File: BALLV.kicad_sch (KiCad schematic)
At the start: 3 parts

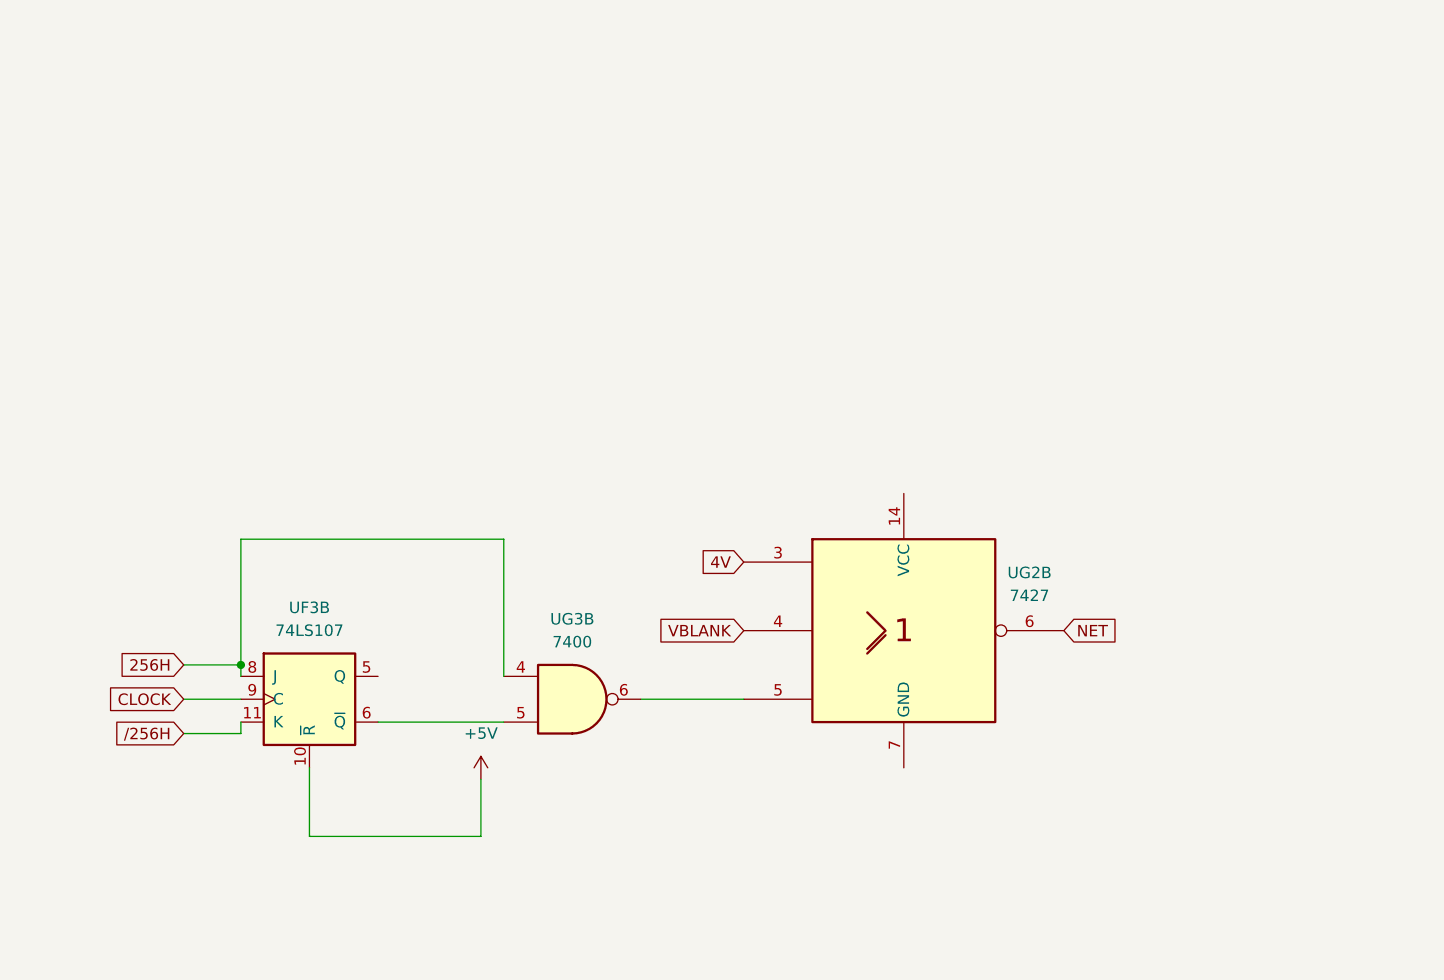
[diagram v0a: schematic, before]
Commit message: Added remainder of sheets
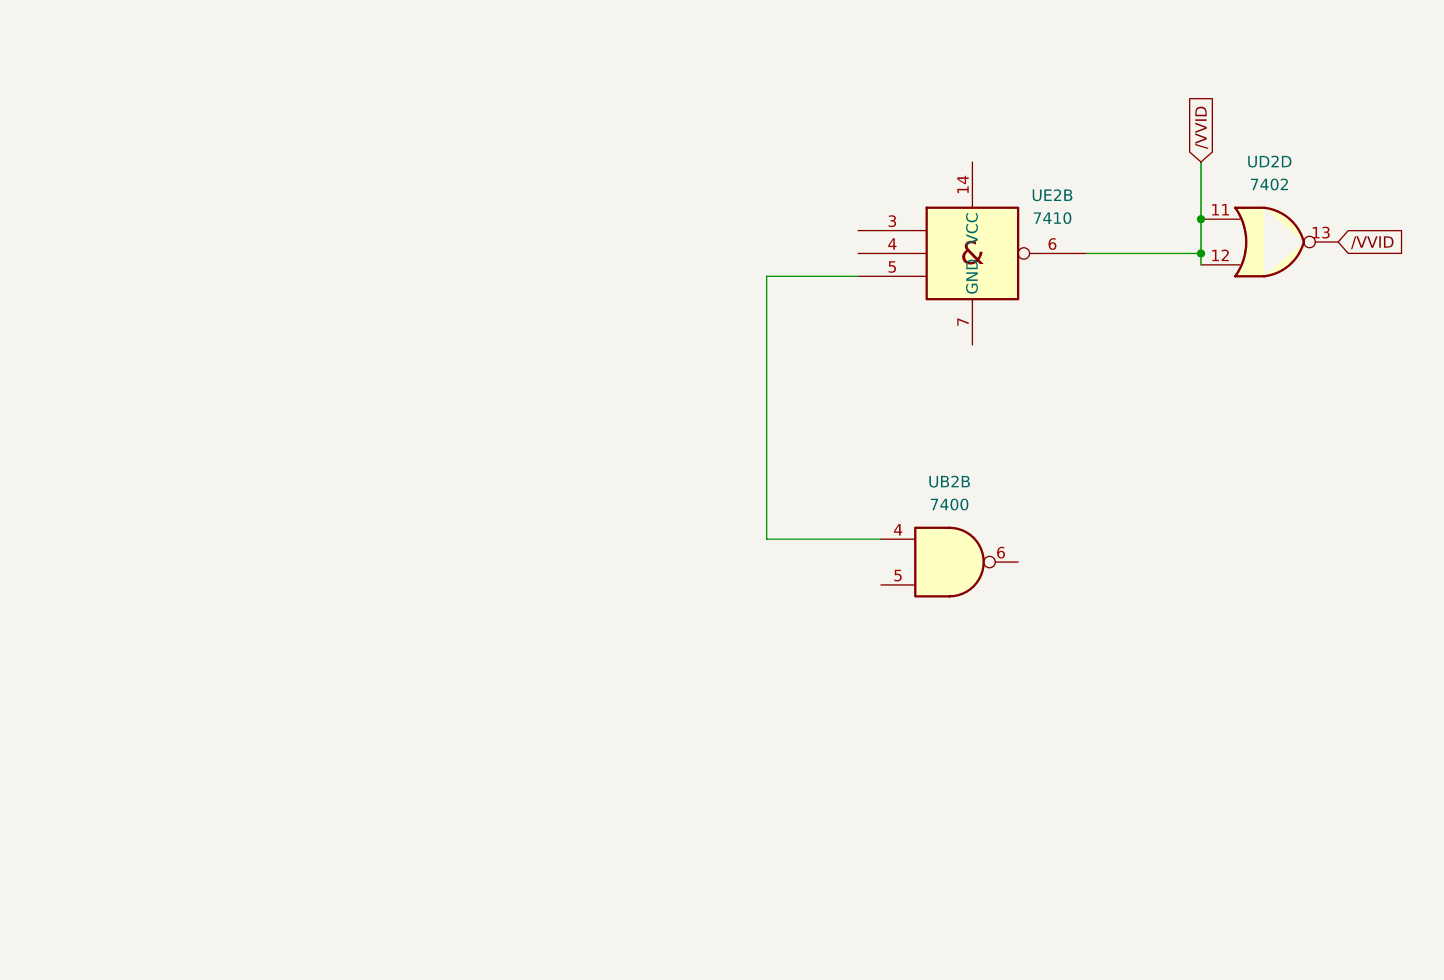
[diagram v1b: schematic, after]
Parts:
- removed UF3: 74LS107, Package_DIP:DIP-14_W7.62mm_Socket_LongPads, symbol 74xx:74LS107
- removed UG2: 7427, Package_DIP:DIP-14_W7.62mm_Socket_LongPads, symbol 74xx_IEEE:7427
- removed UG3: 7400, Package_DIP:DIP-14_W7.62mm_Socket_LongPads, symbol 74xx:7400
- added UB2: 7400, Package_DIP:DIP-14_W7.62mm_Socket_LongPads, symbol 74xx:7400
- added UD2: 7402, Package_DIP:DIP-14_W7.62mm_Socket_LongPads, symbol 74xx:7402
- added UE2: 7410, Package_DIP:DIP-14_W7.62mm_Socket_LongPads, symbol 74xx_IEEE:7410
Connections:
- new net: UB2.4, UE2.5
- new net /VVID: UD2.11, UD2.12, UD2.13, UE2.6

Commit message: R20260915
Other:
- company: (none) -> Atari
- title: (none) -> PONG
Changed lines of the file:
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@@
 	(generator "eeschema")
 	(generator_version "10.0")
-	(paper "A4")
+	(paper "USLetter")
+	(title_block
+		(title "PONG")
+		(company "Atari")
+	)
 	(junction
 		(at 193.04 50.8)

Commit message: R20260918
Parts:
- UB2, UD2, UE2: footprint Package_DIP:DIP-14_W7.62mm_Socket_LongPads -> pong:pong_DIP-14_W7.62mm_Socket_LongPads
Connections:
- net /VVID: no longer UD2.13
- net +3.3V: now reaches UE2.14 (VCC)
- net GND: now reaches UE2.7 (GND)
- new net VVID: UD2.13
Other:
- note added: "NEED 9316 ICS"
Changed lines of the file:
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@@
 		(company "Atari")
 	)
-	(junction
-		(at 193.04 50.8)
-		(diameter 0)
-		(color 0 0 0 0)
+	(text "NEED 9316 ICS"
+		(exclude_from_sim no)
+		(at 70.104 101.346 0)
+		(effects
+			(font
+				(size 1.27 1.27)
+			)
+		)
 	)
 	(junction
@@
 	(wire
 		(pts
-			(xy 193.04 44.45) (xy 193.04 50.8)
+			(xy 154.94 57.15) (xy 144.78 57.15)
 		)
 		(stroke
@@
 		)
 	)
-	(wire
-		(pts
-			(xy 154.94 57.15) (xy 144.78 57.15)
-		)
-		(stroke
-			(width 0)
-			(type default)
-		)
-	)
 	(global_label "{slash}VVID"
 		(shape input)
-		(at 193.04 44.45 90)
+		(at 193.04 50.8 90)
 		(fields_autoplaced yes)
 		(effects
@@
 		)
 		(property "Intersheetrefs" "${INTERSHEET_REFS}"
-			(at 193.04 36.0823 90)
+			(at 193.04 42.4323 90)
 			(hide yes)
 			(show_name no)
@@
 		)
 	)
-	(global_label "{slash}VVID"
+	(global_label "VVID"
 		(shape input)
 		(at 208.28 53.34 0)
@@
 			)
 		)
-		(property "Footprint" "Package_DIP:DIP-14_W7.62mm_Socket_LongPads"
+		(property "Footprint" "pong:pong_DIP-14_W7.62mm_Socket_LongPads"
 			(at 200.66 53.34 0)
 			(hide yes)
@@
 					(reference "UD2")
 					(unit 4)
+				)
+			)
+		)
+	)
+	(symbol
+		(lib_id "power:GND")
+		(at 167.64 64.77 0)
+		(unit 1)
+		(body_style 1)
+		(exclude_from_sim no)
+		(in_bom yes)
+		(on_board yes)
+		(in_pos_files yes)
+		(dnp no)
+		(property "Reference" "#PWR0143"
+			(at 167.64 71.12 0)
+			(hide yes)
+			(show_name no)
+			(do_not_autoplace no)
+			(effects
+				(font
+					(size 1.27 1.27)
+				)
+			)
+		)
+		(property "Value" "GND"
+			(at 170.434 63.754 90)
+			(show_name no)
+			(do_not_autoplace no)
+			(effects
+				(font
+					(size 1.27 1.27)
+				)
+				(justify right)
+			)
+		)
+		(property "Footprint" ""
+			(at 167.64 64.77 0)
+			(hide yes)
+			(show_name no)
+			(do_not_autoplace no)
+			(effects
+				(font
+					(size 1.27 1.27)
+				)
+			)
+		)
+		(property "Datasheet" ""
+			(at 167.64 64.77 0)
+			(hide yes)
+			(show_name no)
+			(do_not_autoplace no)
+			(effects
+				(font
+					(size 1.27 1.27)
+				)
+			)
+		)
+		(property "Description" "Power symbol creates a global label with name \"GND\" , ground"
+			(at 167.64 64.77 0)
+			(hide yes)
+			(show_name no)
+			(do_not_autoplace no)
+			(effects
+				(font
+					(size 1.27 1.27)
+				)
+			)
+		)
+		(pin "1"
+		)
+		(instances
+			(project "pong"
+				(path "/6c55baa6-be38-444e-ac95-9cecf812b759/77c55ca7-a066-4d98-a4d1-18b720a3c31f"
+					(reference "#PWR0143")
+					(unit 1)
 				)
 			)
@@
 			)
 		)
-		(property "Footprint" "Package_DIP:DIP-14_W7.62mm_Socket_LongPads"
+		(property "Footprint" "pong:pong_DIP-14_W7.62mm_Socket_LongPads"
 			(at 165.1 88.9 0)
 			(hide yes)
@@
 			)
 		)
-		(property "Footprint" "Package_DIP:DIP-14_W7.62mm_Socket_LongPads"
+		(property "Footprint" "pong:pong_DIP-14_W7.62mm_Socket_LongPads"
 			(at 167.64 54.61 0)
 			(hide yes)
@@
 				)
 			)
+		)
+	)
+	(symbol
+		(lib_id "power:VCC")
+		(at 167.64 44.45 0)
+		(unit 1)
+		(body_style 1)
+		(exclude_from_sim no)
+		(in_bom yes)
+		(on_board yes)
+		(in_pos_files yes)
+		(dnp no)
+		(fields_autoplaced yes)
+		(property "Reference" "#PWR0142"
+			(at 167.64 48.26 0)
+			(hide yes)
+			(show_name no)
+			(do_not_autoplace no)
+			(effects
+				(font
+					(size 1.27 1.27)
+				)
+			)
+		)
+		(property "Value" "+3.3V"
+			(at 167.6399 40.64 90)
+			(show_name no)
+			(do_not_autoplace no)
+			(effects
+				(font
+					(size 1.27 1.27)
+				)
+				(justify left)
+			)
+		)
+		(property "Footprint" ""
+			(at 167.64 44.45 0)
+			(hide yes)
+			(show_name no)
+			(do_not_autoplace no)
+			(effects
+				(font
+					(size 1.27 1.27)
+				)
+			)
+		)
+		(property "Datasheet" ""
+			(at 167.64 44.45 0)
+			(hide yes)
+			(show_name no)
+			(do_not_autoplace no)
+			(effects
+				(font
+					(size 1.27 1.27)
+				)
+			)
+		)
+		(property "Description" "Power symbol creates a global label with name \"VCC\""
+			(at 167.64 44.45 0)
+			(hide yes)
+			(show_name no)
+			(do_not_autoplace no)
+			(effects
+				(font
+					(size 1.27 1.27)
+				)
+			)
+		)
+		(pin "1"
+		)
+		(instances
+			(project "pong"
+				(path "/6c55baa6-be38-444e-ac95-9cecf812b759/77c55ca7-a066-4d98-a4d1-18b720a3c31f"
+					(reference "#PWR0142")
+					(unit 1)
+				)
+			)

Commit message: R20260922PM
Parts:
- added UA3, UB3: 74LS161, pong:pong_DIP-16_W7.62mm_Socket_LongPads, symbol 74xx:74LS161
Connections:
- net +3.3V: now also UA3.16 (VCC), UB3.16 (VCC)
- net GND: now also UA3.3 (D0), UA3.4 (D1), UA3.5 (D2), UA3.6 (D3), UA3.8 (GND), UB3.8 (GND)
- net at UB2.4, UE2.5: now also UA3.15 (TC)
- net at UB2.5: now also UA3.7 (CEP), UB3.15 (TC)
- net at UB2.6: now also UA3.9 (~{PE}), UB3.9 (~{PE})
- net at UE2.3: now also UB3.12 (Q2)
- net at UE2.4: now also UB3.11 (Q3)
- new net: UA3.1 (~{MR}), UA3.10 (CET), UB3.1 (~{MR}), UB3.7 (CEP)
- new net A6: UB3.3 (D0)
- new net B6: UB3.4 (D1)
- new net C6: UB3.5 (D2)
- new net D6: UB3.6 (D3)
- new net /HSYNC: UA3.2 (CP), UB3.2 (CP)
- new net /VBLANK: UB3.10 (CET)
- no-connect marks 0 -> 6
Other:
- note removed: "NEED 9316 ICS"
- moved on the sheet: UB2B
